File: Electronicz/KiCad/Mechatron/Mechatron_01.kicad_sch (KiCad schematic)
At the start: 45 parts, among them J1 Conn_01x15_Socket, J10 Servo_1, J11 Servo_2, J12 Servo_3, J13 V_ESP32, J14 GND_ESP32, J15 Motor_1, J16 Motor_2, J17 Motor_3, J18 Motor_4, J19 V_LED_2, J2 US_Sensor1, J20 V_LED_1, J21 V_LED_top, J22 GND_LED_top, J23 GND_LED_2, J24 GND_LED_1, J25 Conn_01x06_Socket, J3 US_sensor_2, J4 US_sensor3, J5 US_sensor4, J6 US_sensor5, J7 US_sensor6, J8 GND_Battery, J9 V_Battery_Switch, Q1 LR_LED_Sensors, Q2 LR_3, Q3 LR_2, Q4 LR_1, Q5 LED_top, Q6 LED_2, Q7 LED_1

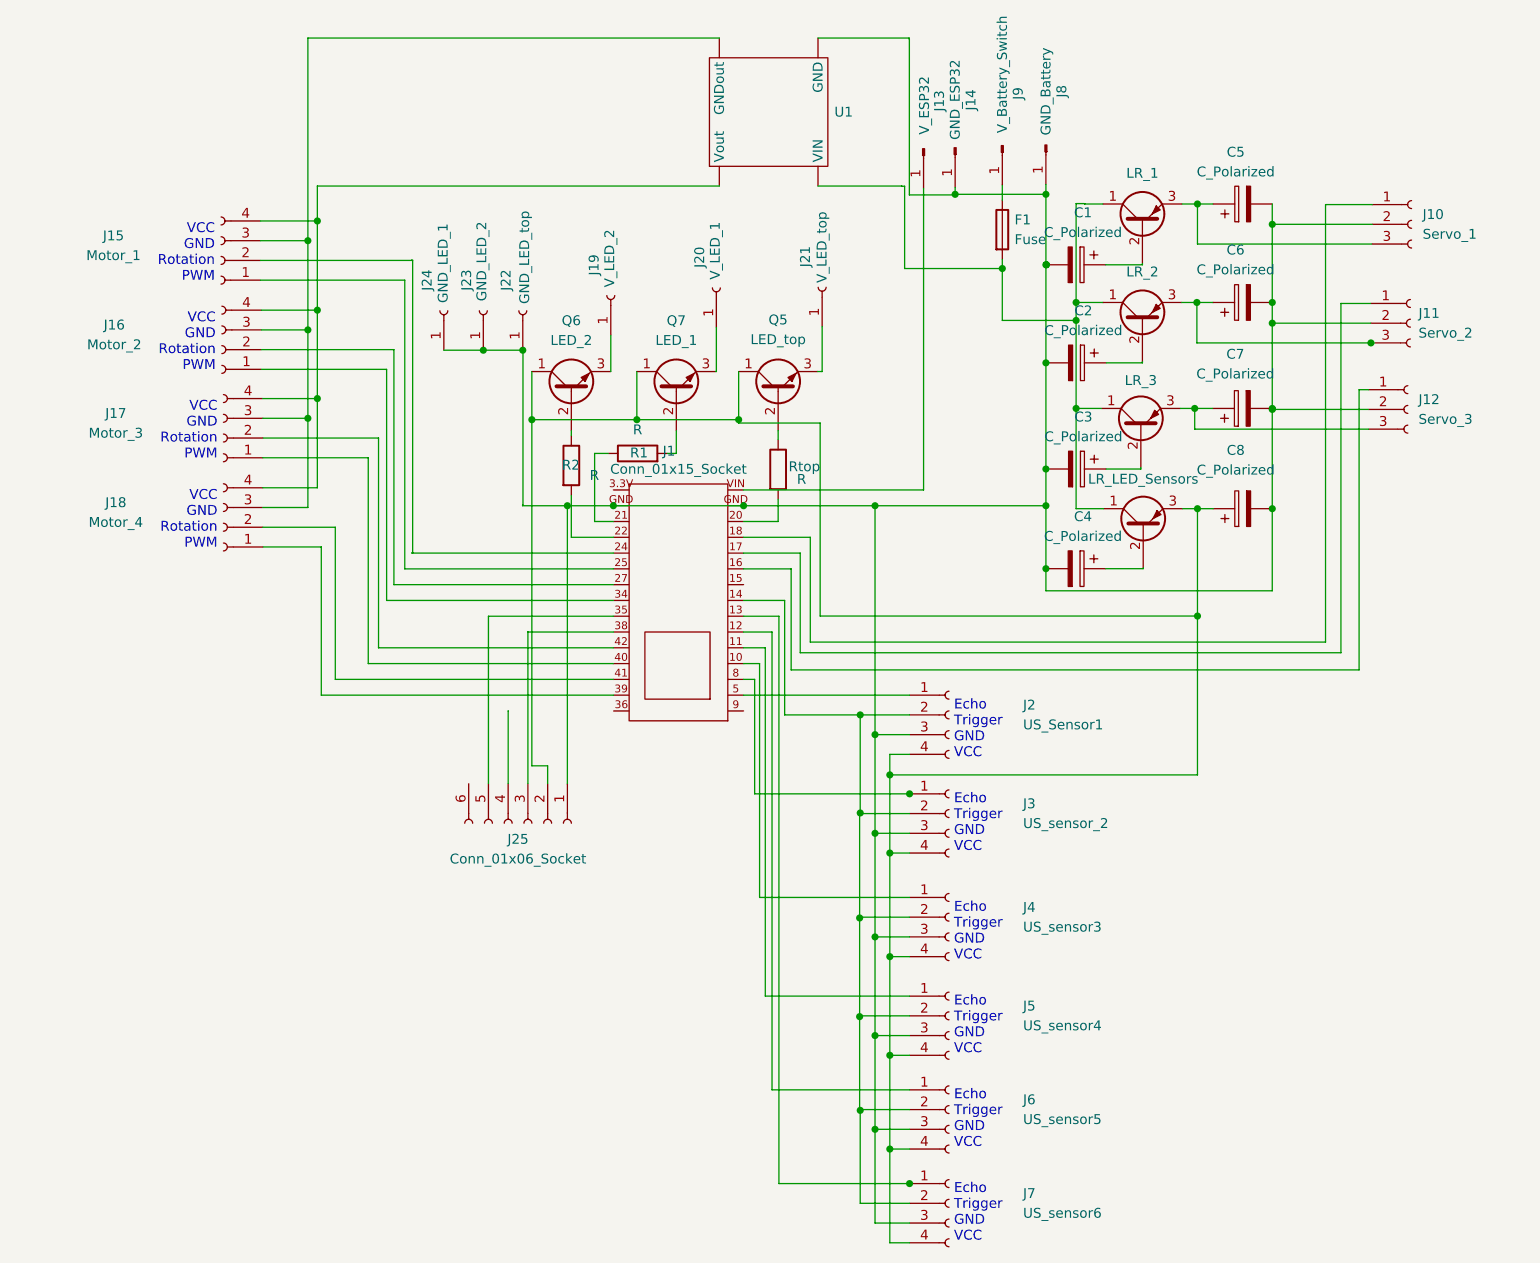
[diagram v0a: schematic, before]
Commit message: KiCad Footprint zuweisen
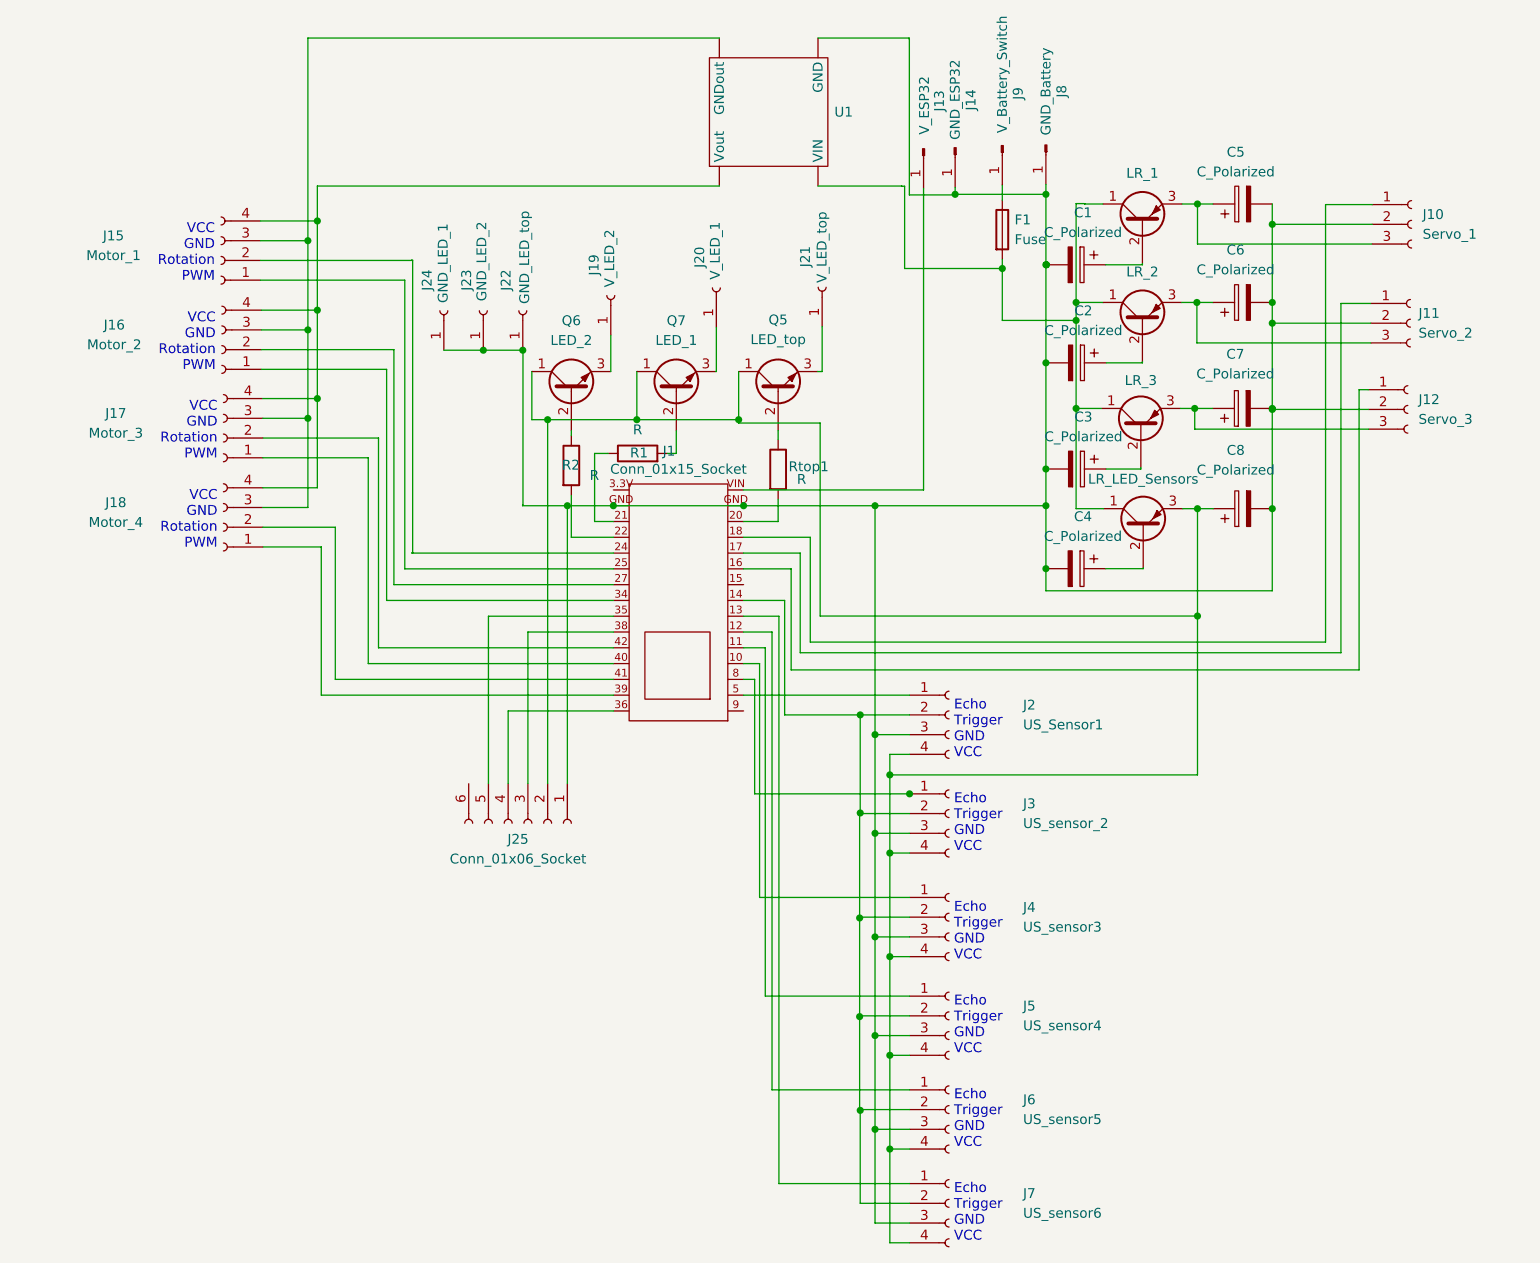
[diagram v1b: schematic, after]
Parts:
- J1: footprint (none) -> Library:ESP32
- J10, J11, J12: footprint (none) -> Connector_PinSocket_2.54mm:PinSocket_1x03_P2.54mm_Vertical
- J13, J14, J8, J9: footprint (none) -> Connector_PinHeader_2.54mm:PinHeader_1x01_P2.54mm_Vertical
- J15, J16, J17, J18, J2, J3, J4, J5, J6, J7: footprint (none) -> Connector_PinSocket_2.54mm:PinSocket_1x04_P2.54mm_Vertical
- J19, J20, J21, J22, J23, J24: footprint (none) -> Connector_PinSocket_2.54mm:PinSocket_1x01_P2.54mm_Vertical
- J25: footprint (none) -> Connector_PinSocket_2.54mm:PinSocket_1x06_P2.54mm_Vertical
- R1, R2: footprint (none) -> Resistor_THT:R_Axial_DIN0207_L6.3mm_D2.5mm_P10.16mm_Horizontal
- Rtop1: renamed from Rtop; footprint (none) -> Resistor_THT:R_Axial_DIN0207_L6.3mm_D2.5mm_P10.16mm_Horizontal
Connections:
- net at J25.4 (Pin_4): now also J1.36

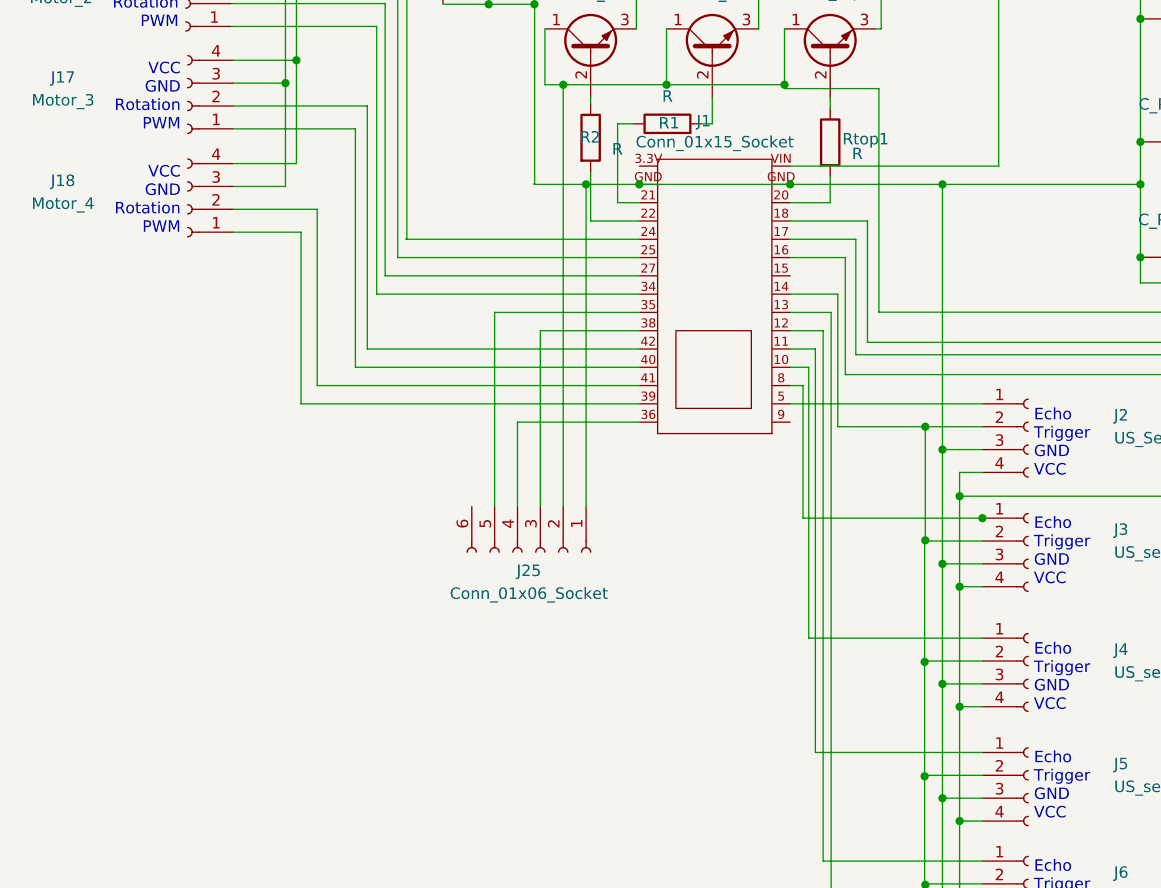
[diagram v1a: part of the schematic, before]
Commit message: add amplifier and speaker pins
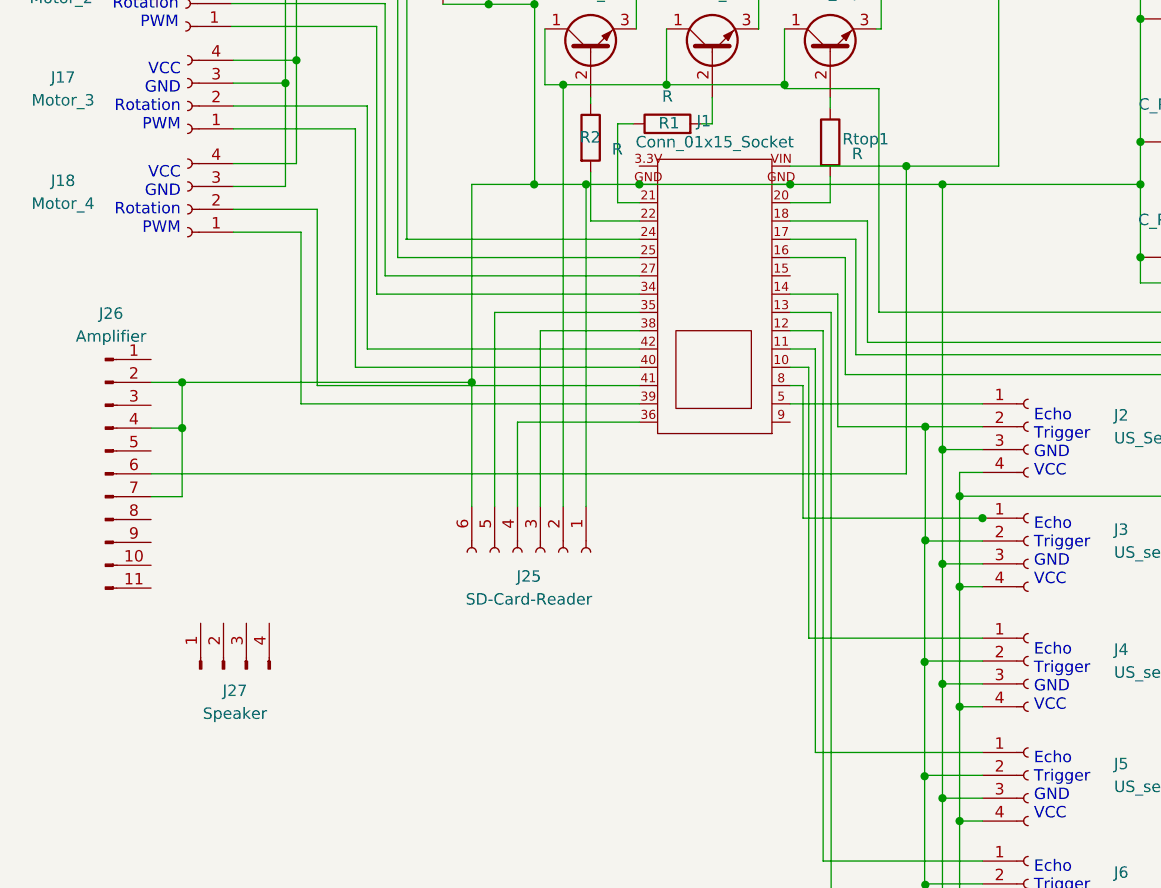
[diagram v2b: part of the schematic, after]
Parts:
- added J26: Amplifier, symbol Connector:Conn_01x11_Pin
- added J27: Speaker, symbol Connector:Conn_01x04_Pin
- J25: value Conn_01x06_Socket -> SD-Card-Reader
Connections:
- net at C1.2, C2.2, C3.2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: now also J25.6 (Pin_6), J26.2 (Pin_2), J26.4 (Pin_4), J26.7 (Pin_7)
- net at J1.VIN, J13.1 (Pin_1): now also J26.6 (Pin_6)
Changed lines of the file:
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@@
   (junction (at 172.9486 39.5986) (diameter 0) (color 0 0 0 0)
   )
+  (junction (at 37.338 102.8954) (diameter 0) (color 0 0 0 0)
+  )
   (junction (at 143.8148 35.7378) (diameter 0) (color 0 0 0 0)
   )
@@
   (junction (at 172.9486 49.657) (diameter 0) (color 0 0 0 0)
   )
+  (junction (at 117.8052 73.787) (diameter 0) (color 0 0 0 0)
+  )
   (junction (at 121.8184 156.083) (diameter 0) (color 0 0 0 0)
   )
@@
   (junction (at 48.8188 53.1876) (diameter 0) (color 0 0 0 0)
   )
+  (junction (at 37.338 97.8154) (diameter 0) (color 0 0 0 0)
+  )
   (junction (at 104.267 64.7446) (diameter 0) (color 0 0 0 0)
   )
@@
   (junction (at 147.701 63.2968) (diameter 0) (color 0 0 0 0)
   )
+  (junction (at 69.5198 97.8154) (diameter 0) (color 0 0 0 0)
+  )
   (junction (at 119.9134 102.743) (diameter 0) (color 0 0 0 0)
   )
@@
   (junction (at 50.038 39.1668) (diameter 0) (color 0 0 0 0)
   )
+  (junction (at 76.454 75.819) (diameter 0) (color 0 0 0 0)
+  )
   (junction (at 82.2198 75.819) (diameter 0) (color 0 0 0 0)
   )
@@
     (stroke (width 0) (type default))
   )
+  (wire (pts (xy 37.338 110.5154) (xy 33.8836 110.5154))
+    (stroke (width 0) (type default))
+  )
   (wire (pts (xy 96.2406 66.167) (xy 96.2406 69.088))
     (stroke (width 0) (type default))
   )
-  (wire (pts (xy 128.0668 73.787) (xy 104.902 73.787))
+  (wire (pts (xy 128.0668 73.787) (xy 117.8052 73.787))
     (stroke (width 0) (type default))
   )
@@
     (stroke (width 0) (type default))
   )
+  (wire (pts (xy 76.454 75.819) (xy 82.2198 75.819))
+    (stroke (width 0) (type default))
+  )
   (wire (pts (xy 138.2014 45.2882) (xy 125.6284 45.2882))
     (stroke (width 0) (type default))
@@
     (stroke (width 0) (type default))
   )
+  (wire (pts (xy 33.8836 107.9754) (xy 117.8052 107.9754))
+    (stroke (width 0) (type default))
+  )
   (wire (pts (xy 128.0668 34.9504) (xy 128.0668 73.787))
     (stroke (width 0) (type default))
@@
     (stroke (width 0) (type default))
   )
+  (wire (pts (xy 37.338 102.8954) (xy 33.8836 102.8954))
+    (stroke (width 0) (type default))
+  )
   (wire (pts (xy 172.9486 63.2968) (xy 172.9486 63.4238))
     (stroke (width 0) (type default))
@@
     (stroke (width 0) (type default))
   )
+  (wire (pts (xy 69.5198 75.819) (xy 76.454 75.819))
+    (stroke (width 0) (type default))
+  )
   (wire (pts (xy 126.2634 107.823) (xy 123.7234 107.823))
     (stroke (width 0) (type default))
@@
     (stroke (width 0) (type default))
   )
+  (wire (pts (xy 117.8052 73.787) (xy 104.902 73.787))
+    (stroke (width 0) (type default))
+  )
   (wire (pts (xy 82.7278 66.167) (xy 82.7278 66.8274))
     (stroke (width 0) (type default))
@@
     (stroke (width 0) (type default))
   )
+  (wire (pts (xy 69.5198 97.8154) (xy 69.5198 75.819))
+    (stroke (width 0) (type default))
+  )
   (wire (pts (xy 126.2888 112.903) (xy 126.2634 112.903))
     (stroke (width 0) (type default))
@@
     (stroke (width 0) (type default))
   )
+  (wire (pts (xy 117.8052 107.9754) (xy 117.8052 73.787))
+    (stroke (width 0) (type default))
+  )
   (wire (pts (xy 48.8188 41.7068) (xy 48.8188 53.1876))
     (stroke (width 0) (type default))
@@
     (stroke (width 0) (type default))
   )
+  (wire (pts (xy 33.8836 97.8154) (xy 37.338 97.8154))
+    (stroke (width 0) (type default))
+  )
   (wire (pts (xy 147.701 63.2968) (xy 147.701 76.2))
     (stroke (width 0) (type default))
@@
     (stroke (width 0) (type default))
   )
+  (wire (pts (xy 37.338 97.8154) (xy 37.338 102.8954))
+    (stroke (width 0) (type default))
+  )
   (wire (pts (xy 121.8184 131.318) (xy 121.8184 117.983))
     (stroke (width 0) (type default))
@@
     (stroke (width 0) (type default))
   )
+  (wire (pts (xy 69.5198 111.6076) (xy 69.5198 97.8154))
+    (stroke (width 0) (type default))
+  )
   (wire (pts (xy 106.3244 98.171) (xy 104.902 98.171))
     (stroke (width 0) (type default))
@@
     (stroke (width 0) (type default))
   )
+  (wire (pts (xy 37.338 97.8154) (xy 69.5198 97.8154))
+    (stroke (width 0) (type default))
+  )
   (wire (pts (xy 163.322 90.0176) (xy 163.322 110.4646))
     (stroke (width 0) (type default))
@@
     (stroke (width 0) (type default))
   )
+  (wire (pts (xy 37.338 102.8954) (xy 37.338 110.5154))
+    (stroke (width 0) (type default))
+  )
   (wire (pts (xy 181.7878 94.742) (xy 181.7878 49.784))
     (stroke (width 0) (type default))
@@
   )
   (wire (pts (xy 82.2198 75.819) (xy 82.2198 111.6076))
-    (stroke (width 0) (type default))
-  )
-  (wire (pts (xy 76.454 75.819) (xy 82.2198 75.819))
     (stroke (width 0) (type default))
   )
@@
   (text "VCC\nGND\nRotation\nPWM" (at 37.1856 81.4832 0)
     (effects (font (size 1.27 1.27)) (justify right bottom))
+  )
+  (symbol (lib_id "Connector:Conn_01x11_Pin") (at 28.8036 107.9754 0) (unit 1)
+    (in_bom yes) (on_board yes) (dnp no) (fields_autoplaced)
+    (property "Reference" "J26" (at 29.4386 90.17 0)
+      (effects (font (size 1.27 1.27)))
+    )
+    (property "Value" "Amplifier" (at 29.4386 92.71 0)
+      (effects (font (size 1.27 1.27)))
+    )
+    (property "Footprint" "" (at 28.8036 107.9754 0)
+      (effects (font (size 1.27 1.27)) hide)
+    )
+    (property "Datasheet" "~" (at 28.8036 107.9754 0)
+      (effects (font (size 1.27 1.27)) hide)
+    )
+    (pin "1")
+    (pin "10")
+    (pin "11")
+    (pin "2")
+    (pin "3")
+    (pin "4")
+    (pin "5")
+    (pin "6")
+    (pin "7")
+    (pin "8")
+    (pin "9")
+    (instances
+      (project "Mechatron_01"
+        (path "/582de77e-8ad8-4f99-9634-2e14a1116267"
+          (reference "J26") (unit 1)
+        )
+      )
+    )
   )
   (symbol (lib_id "Connector:Conn_01x04_Socket") (at 37.7444 55.7276 180) (unit 1)
@@
     )
   )
+  (symbol (lib_id "Connector:Conn_01x04_Pin") (at 41.9354 129.667 90) (unit 1)
+    (in_bom yes) (on_board yes) (dnp no) (fields_autoplaced)
+    (property "Reference" "J27" (at 43.2054 132.08 90)
+      (effects (font (size 1.27 1.27)))
+    )
+    (property "Value" "Speaker" (at 43.2054 134.62 90)
+      (effects (font (size 1.27 1.27)))
+    )
+    (property "Footprint" "" (at 41.9354 129.667 0)
+      (effects (font (size 1.27 1.27)) hide)
+    )
+    (property "Datasheet" "~" (at 41.9354 129.667 0)
+      (effects (font (size 1.27 1.27)) hide)
+    )
+    (pin "1")
+    (pin "2")
+    (pin "3")
+    (pin "4")
+    (instances
+      (project "Mechatron_01"
+        (path "/582de77e-8ad8-4f99-9634-2e14a1116267"
+          (reference "J27") (unit 1)
+        )
+      )
+    )
+  )
   (symbol (lib_id "Connector:Conn_01x04_Socket") (at 37.6428 44.2468 180) (unit 1)
     (in_bom yes) (on_board yes) (dnp no)
@@
   (symbol (lib_id "Connector:Conn_01x06_Socket") (at 77.1398 116.6876 270) (unit 1)
     (in_bom yes) (on_board yes) (dnp no) (fields_autoplaced)
-    (property "Reference" "J25" (at 75.8698 118.745 90)
-      (effects (font (size 1.27 1.27)))
-    )
-    (property "Value" "Conn_01x06_Socket" (at 75.8698 121.285 90)
-      (effects (font (size 1.27 1.27)))
-    )
+    (property "Reference" "J25" (at 75.8698 119.38 90)
+      (effects (font (size 1.27 1.27)))
+    )
+    (property "Value" "SD-Card-Reader" (at 75.8698 121.92 90)
+      (effects (font (size 1.27 1.27)))
+    )

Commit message: add TODO
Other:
- note added: "Low Passfilter and amplifier between Esp and In R and L"
- note added: "Trennbar durch Hauptschalter"
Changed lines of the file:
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@@
     (stroke (width 0) (type default))
+  )
+  (text "Trennbar durch Hauptschalter" (at 62.23 33.02 0)
+    (effects (font (size 1.27 1.27)) (justify left bottom))
   )
   (text "Echo\nTrigger\nGND\nVCC" (at 131.9784 120.523 0)
@@
     (effects (font (size 1.27 1.27)) (justify right bottom))
   )
+  (text "Low Passfilter and amplifier\nbetween Esp and In R and L"
+    (at 40.64 104.14 0)
+    (effects (font (size 1.27 1.27)) (justify left bottom))
+  )
   (text "VCC\nGND\nRotation\nPWM" (at 37.1856 70.0024 0)
